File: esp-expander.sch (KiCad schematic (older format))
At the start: 0 parts

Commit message: Added labels
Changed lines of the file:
@@
 $EndDescr
 $Sheet
-S 4950 2700 1750 1850
+S 4250 2550 2250 3350
 U 6212150F
 F0 "ESP32" 50
 F1 "ESP32.sch" 50
+F2 "RESET" I L 4250 2650 50
+F3 "PROG_GPIO0" I L 4250 2750 50
+F4 "PROG_TX" I L 4250 2850 50
+F5 "PROG_RX" I L 4250 2950 50
+F6 "I2C_SCL" I R 6500 2750 50
+F7 "I2C_SDA" I R 6500 2650 50
+F8 "LAN_CLKIN" I L 4250 3250 50
+F9 "LAN_MDC" I L 4250 3350 50
+F10 "LAN_MDIO" I L 4250 3450 50
+F11 "LAN_MODE2" I L 4250 3550 50
+F12 "LAN_MODE1" I L 4250 3650 50
+F13 "LAN_MODE0" I L 4250 3750 50
+F14 "LAN_TXEN" I L 4250 3850 50
+F15 "LAN_TXED1" I L 4250 3950 50
+F16 "LAN_TXED0" I L 4250 4050 50
+F17 "LAN_RESET" I L 4250 4150 50
+F18 "DIGITAL_1" I L 4250 4450 50
+F19 "DIGITAL_2" I L 4250 4550 50
+F20 "DIGITAL_3" I L 4250 4650 50
+F21 "DIGITAL_4" I L 4250 4750 50
+F22 "DIGITAL_5" I L 4250 4850 50
+F23 "MCP_INTA" I R 6500 2850 50
+F24 "MCP_INTB" I R 6500 2950 50
 $EndSheet
 $Sheet
-S 2050 2000 900  1050
+S 4250 1250 900  1050
 U 6213DFD4
 F0 "Power" 50
@@
 $EndSheet
 $Sheet
-S 2250 4850 850  1650
+S 6550 2550 850  1650
 U 6215A73B
 F0 "MCP" 50
 F1 "MCP.sch" 50
+F2 "SDA" I L 6550 2650 50
+F3 "SCL" I L 6550 2750 50
+F4 "INTB" I L 6550 2950 50
+F5 "INTA" I L 6550 2850 50
+F6 "MCP1" I R 7400 2650 50
+F7 "MCP2" I R 7400 2750 50
+F8 "MCP3" I R 7400 2850 50
+F9 "MCP4" I R 7400 2950 50
+F10 "MCP5" I R 7400 3050 50
+F11 "MCP6" I R 7400 3150 50
+F12 "MCP7" I R 7400 3250 50
+F13 "MCP8" I R 7400 3350 50
+F14 "MCP9" I R 7400 3450 50
+F15 "MCP10" I R 7400 3550 50
+F16 "MCP11" I R 7400 3650 50
+F17 "MCP12" I R 7400 3750 50
+F18 "MCP13" I R 7400 3850 50
+F19 "MCP14" I R 7400 3950 50
+F20 "MCP15" I R 7400 4050 50
+F21 "MCP16" I R 7400 4150 50
 $EndSheet
 $EndSCHEMATC

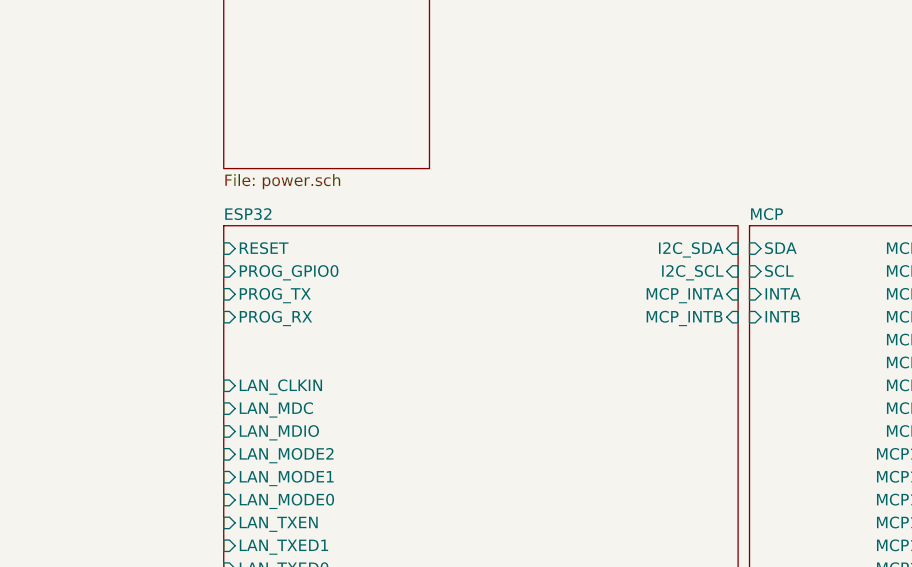
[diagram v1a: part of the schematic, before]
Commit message: Added programming port
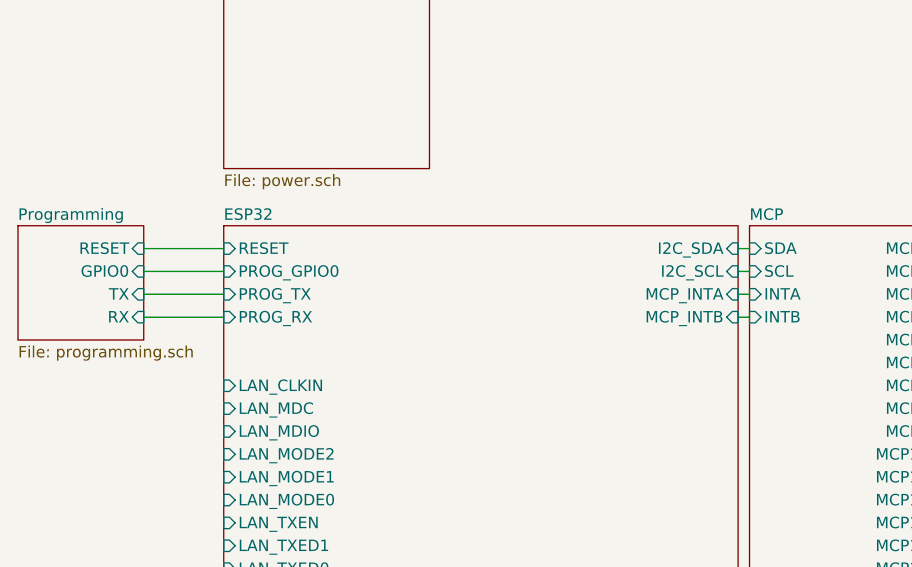
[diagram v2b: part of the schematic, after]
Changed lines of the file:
@@
 $Descr A4 11693 8268
 encoding utf-8
-Sheet 1 4
+Sheet 1 5
 Title "ESP Expander"
 Date "2022-02-20"
@@
 F21 "MCP16" I R 7400 4150 50
 $EndSheet
+$Sheet
+S 3350 2550 550  500
+U 62173728
+F0 "Programming" 50
+F1 "programming.sch" 50
+F2 "RX" I R 3900 2950 50
+F3 "TX" I R 3900 2850 50
+F4 "GPIO0" I R 3900 2750 50
+F5 "RESET" I R 3900 2650 50
+$EndSheet
+Wire Wire Line
+	3900 2650 4250 2650
+Wire Wire Line
+	4250 2750 3900 2750
+Wire Wire Line
+	3900 2850 4250 2850
+Wire Wire Line
+	4250 2950 3900 2950
+Wire Wire Line
+	6500 2650 6550 2650
+Wire Wire Line
+	6500 2750 6550 2750
+Wire Wire Line
+	6500 2850 6550 2850
+Wire Wire Line
+	6500 2950 6550 2950
 $EndSCHEMATC

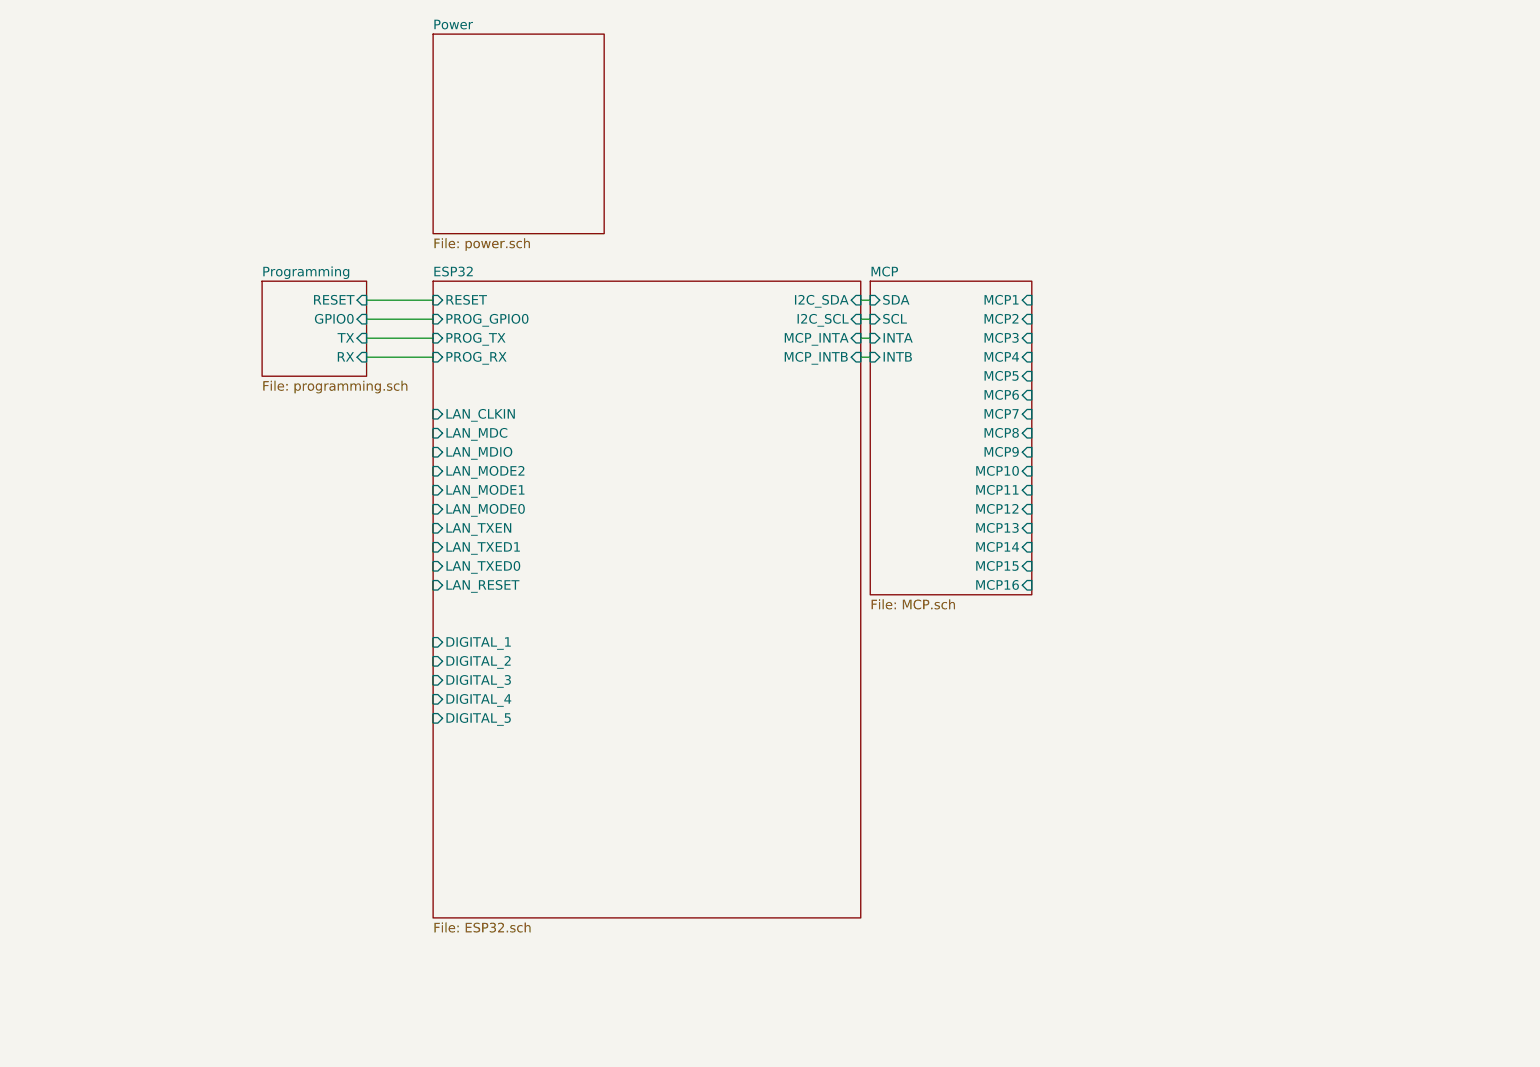
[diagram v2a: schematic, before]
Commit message: Added LAN circuit
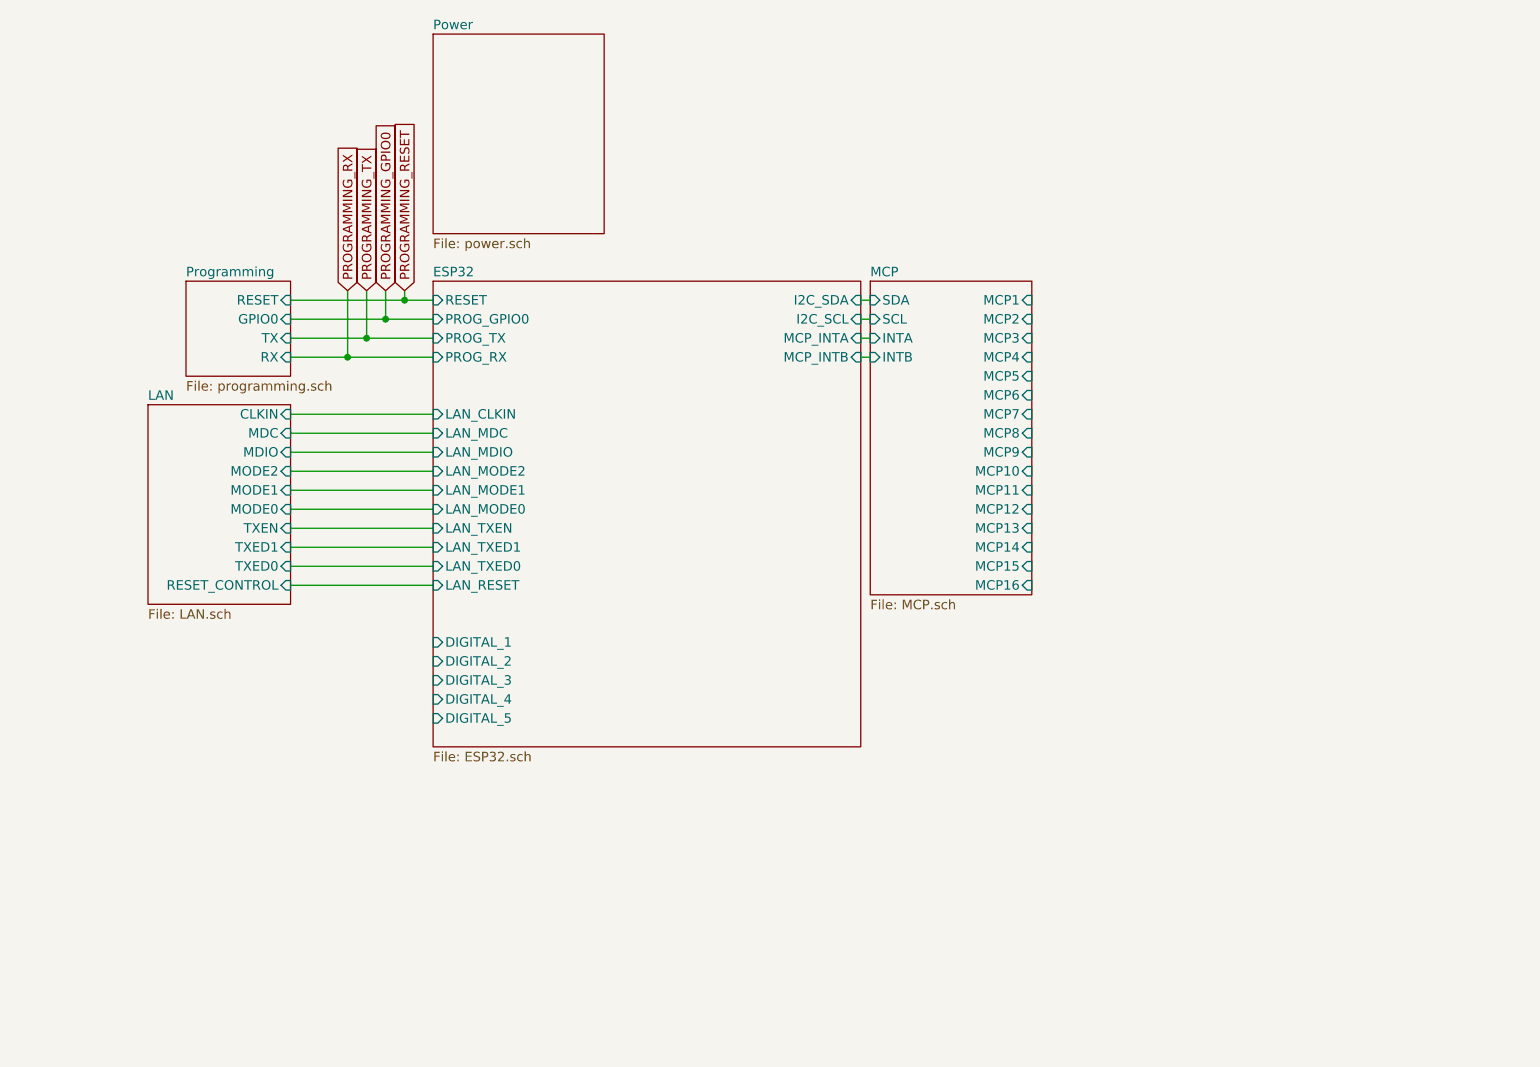
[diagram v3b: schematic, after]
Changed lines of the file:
@@
 $Descr A4 11693 8268
 encoding utf-8
-Sheet 1 5
+Sheet 1 6
 Title "ESP Expander"
 Date "2022-02-20"
@@
 $EndDescr
 $Sheet
-S 4250 2550 2250 3350
+S 4250 2550 2250 2450
 U 6212150F
 F0 "ESP32" 50
@@
 $EndSheet
 $Sheet
-S 3350 2550 550  500
+S 2950 2550 550  500
 U 62173728
 F0 "Programming" 50
 F1 "programming.sch" 50
-F2 "RX" I R 3900 2950 50
-F3 "TX" I R 3900 2850 50
-F4 "GPIO0" I R 3900 2750 50
-F5 "RESET" I R 3900 2650 50
+F2 "RX" I R 3500 2950 50
+F3 "TX" I R 3500 2850 50
+F4 "GPIO0" I R 3500 2750 50
+F5 "RESET" I R 3500 2650 50
 $EndSheet
-Wire Wire Line
-	3900 2650 4250 2650
-Wire Wire Line
-	4250 2750 3900 2750
-Wire Wire Line
-	3900 2850 4250 2850
-Wire Wire Line
-	4250 2950 3900 2950
 Wire Wire Line
 	6500 2650 6550 2650
@@
 Wire Wire Line
 	6500 2950 6550 2950
+$Sheet
+S 2750 3200 750  1050
+U 62182BE5
+F0 "LAN" 50
+F1 "LAN.sch" 50
+F2 "TXED0" I R 3500 4050 50
+F3 "TXED1" I R 3500 3950 50
+F4 "TXEN" I R 3500 3850 50
+F5 "MODE0" I R 3500 3750 50
+F6 "MODE1" I R 3500 3650 50
+F7 "MODE2" I R 3500 3550 50
+F8 "MDIO" I R 3500 3450 50
+F9 "MDC" I R 3500 3350 50
+F10 "CLKIN" I R 3500 3250 50
+F11 "RESET_CONTROL" I R 3500 4150 50
+$EndSheet
+Text GLabel 4100 2600 1    50   Input ~ 0
+PROGRAMMING_RESET
+Text GLabel 4000 2600 1    50   Input ~ 0
+PROGRAMMING_GPIO0
+Text GLabel 3900 2600 1    50   Input ~ 0
+PROGRAMMING_TX
+Text GLabel 3800 2600 1    50   Input ~ 0
+PROGRAMMING_RX
+Wire Wire Line
+	3500 2750 4000 2750
+Wire Wire Line
+	3500 2850 3900 2850
+Wire Wire Line
+	3500 2950 3800 2950
+Wire Wire Line
+	4100 2600 4100 2650
+Connection ~ 4100 2650
+Wire Wire Line
+	4100 2650 4250 2650
+Wire Wire Line
+	4000 2600 4000 2750
+Connection ~ 4000 2750
+Wire Wire Line
+	4000 2750 4250 2750
+Wire Wire Line
+	3900 2600 3900 2850
+Connection ~ 3900 2850
+Wire Wire Line
+	3900 2850 4250 2850
+Wire Wire Line
+	3500 2650 4100 2650
+Wire Wire Line
+	3800 2600 3800 2950
+Connection ~ 3800 2950
+Wire Wire Line
+	3800 2950 4250 2950
+Wire Wire Line
+	3500 3250 4250 3250
+Wire Wire Line
+	4250 3350 3500 3350
+Wire Wire Line
+	3500 3450 4250 3450
+Wire Wire Line
+	4250 3550 3500 3550
+Wire Wire Line
+	3500 3650 4250 3650
+Wire Wire Line
+	4250 3750 3500 3750
+Wire Wire Line
+	3500 3850 4250 3850
+Wire Wire Line
+	4250 3950 3500 3950
+Wire Wire Line
+	3500 4050 4250 4050
+Wire Wire Line
+	4250 4150 3500 4150
 $EndSCHEMATC

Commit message: Added lcsc part nums
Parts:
- added J3, J4: Conn_01x16, Connector_PinHeader_2.54mm:PinHeader_1x16_P2.54mm_Vertical, symbol Connector_Generic:Conn_01x16
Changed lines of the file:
@@
 Wire Wire Line
 	4250 4150 3500 4150
+$Comp
+L Connector_Generic:Conn_01x16 J3
+U 1 1 6223BC0D
+P 9400 2900
+F 0 "J3" H 9480 2892 50  0000 L CNN
+F 1 "Conn_01x16" H 9480 2801 50  0000 L CNN
+F 2 "Connector_PinHeader_2.54mm:PinHeader_1x16_P2.54mm_Vertical" H 9400 2900 50  0001 C CNN
+F 3 "~" H 9400 2900 50  0001 C CNN
+	1    9400 2900
+	1    0    0    -1
+$EndComp
+$Comp
+L Connector_Generic:Conn_01x16 J4
+U 1 1 6223C85B
+P 9400 4700
+F 0 "J4" H 9480 4692 50  0000 L CNN
+F 1 "Conn_01x16" H 9480 4601 50  0000 L CNN
+F 2 "Connector_PinHeader_2.54mm:PinHeader_1x16_P2.54mm_Vertical" H 9400 4700 50  0001 C CNN
+F 3 "~" H 9400 4700 50  0001 C CNN
+	1    9400 4700
+	1    0    0    -1
+$EndComp
 $EndSCHEMATC

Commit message: Added schematic
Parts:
- removed J4: Conn_01x16, Connector_PinHeader_2.54mm:PinHeader_1x16_P2.54mm_Vertical, symbol Connector_Generic:Conn_01x16
- added J4: Conn_01x12, Connector_PinHeader_2.54mm:PinHeader_1x12_P2.54mm_Vertical, symbol Connector_Generic:Conn_01x12
- J3: footprint Connector_PinHeader_2.54mm:PinHeader_1x16_P2.54mm_Vertical -> Connector_PinHeader_2.54mm:PinHeader_1x18_P2.54mm_Vertical; symbol Connector_Generic:Conn_01x16 -> Connector_Generic:Conn_01x18; LCSC (none) -> C725948
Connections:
- net MCP/MCP1: now also J3.2 (Pin_2)
- net MCP/MCP10: now also J3.11 (Pin_11)
- net MCP/MCP11: now also J3.12 (Pin_12)
- net MCP/MCP12: now also J3.13 (Pin_13)
- net MCP/MCP13: now also J3.14 (Pin_14)
- net MCP/MCP14: now also J3.15 (Pin_15)
- net MCP/MCP15: now also J3.16 (Pin_16)
- net MCP/MCP16: now also J3.17 (Pin_17)
- net MCP/MCP2: now also J3.3 (Pin_3)
- net MCP/MCP3: now also J3.4 (Pin_4)
- net MCP/MCP4: now also J3.5 (Pin_5)
- net MCP/MCP5: now also J3.6 (Pin_6)
- net MCP/MCP6: now also J3.7 (Pin_7)
- net MCP/MCP7: now also J3.8 (Pin_8)
- net MCP/MCP8: now also J3.9 (Pin_9)
- net MCP/MCP9: now also J3.10 (Pin_10)
- net PROGRAMMING_GPIO0: now also J4.10 (Pin_10)
- net PROGRAMMING_RESET: now also J4.9 (Pin_9)
- net PROGRAMMING_RX: now also J4.12 (Pin_12)
- net PROGRAMMING_TX: now also J4.11 (Pin_11)
- net +3V3: now reaches J3.1 (Pin_1)
- net +3V3: now also J4.3 (Pin_3)
- new net DIGITAL1: J4.4 (Pin_4)
- new net DIGITAL2: J4.5 (Pin_5)
- new net DIGITAL3: J4.6 (Pin_6)
- new net DIGITAL4: J4.7 (Pin_7)
- new net DIGITAL5: J4.8 (Pin_8)
- new net GND: J3.18 (Pin_18), J4.2 (Pin_2)
- new net VCC: J4.1 (Pin_1)
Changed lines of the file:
@@
 	4250 4150 3500 4150
 $Comp
-L Connector_Generic:Conn_01x16 J3
+L Connector_Generic:Conn_01x18 J3
 U 1 1 6223BC0D
-P 9400 2900
-F 0 "J3" H 9480 2892 50  0000 L CNN
-F 1 "Conn_01x16" H 9480 2801 50  0000 L CNN
-F 2 "Connector_PinHeader_2.54mm:PinHeader_1x16_P2.54mm_Vertical" H 9400 2900 50  0001 C CNN
-F 3 "~" H 9400 2900 50  0001 C CNN
-	1    9400 2900
+P 7650 3350
+F 0 "J3" V 7750 4000 50  0000 L CNN
+F 1 "Conn_01x16" V 7750 2550 50  0000 L CNN
+F 2 "Connector_PinHeader_2.54mm:PinHeader_1x18_P2.54mm_Vertical" H 7650 3350 50  0001 C CNN
+F 3 "~" H 7650 3350 50  0001 C CNN
+F 4 "C725948" H 7650 3350 50  0001 C CNN "LCSC"
+	1    7650 3350
+	1    0    0    -1
+$EndComp
+Wire Wire Line
+	7400 2650 7450 2650
+Wire Wire Line
+	7400 2750 7450 2750
+Wire Wire Line
+	7400 2850 7450 2850
+Wire Wire Line
+	7400 2950 7450 2950
+Wire Wire Line
+	7400 3050 7450 3050
+Wire Wire Line
+	7400 3150 7450 3150
+Wire Wire Line
+	7400 3250 7450 3250
+Wire Wire Line
+	7400 3350 7450 3350
+Wire Wire Line
+	7400 3450 7450 3450
+Wire Wire Line
+	7400 3550 7450 3550
+Wire Wire Line
+	7400 3650 7450 3650
+Wire Wire Line
+	7400 3750 7450 3750
+Wire Wire Line
+	7400 3850 7450 3850
+Wire Wire Line
+	7400 3950 7450 3950
+Wire Wire Line
+	7400 4050 7450 4050
+Wire Wire Line
+	7400 4150 7450 4150
+Text GLabel 7400 5650 0    50   Input ~ 0
+PROGRAMMING_RESET
+Text GLabel 7400 5750 0    50   Input ~ 0
+PROGRAMMING_GPIO0
+Text GLabel 7400 5850 0    50   Input ~ 0
+PROGRAMMING_TX
+Text GLabel 7400 5950 0    50   Input ~ 0
+PROGRAMMING_RX
+Text GLabel 4200 4450 0    50   Input ~ 0
+DIGITAL1
+Text GLabel 4200 4550 0    50   Input ~ 0
+DIGITAL2
+Text GLabel 4200 4650 0    50   Input ~ 0
+DIGITAL3
+Text GLabel 4200 4750 0    50   Input ~ 0
+DIGITAL4
+Text GLabel 4200 4850 0    50   Input ~ 0
+DIGITAL5
+Wire Wire Line
+	4200 4450 4250 4450
+Wire Wire Line
+	4250 4550 4200 4550
+Wire Wire Line
+	4250 4650 4200 4650
+Wire Wire Line
+	4250 4750 4200 4750
+Wire Wire Line
+	4250 4850 4200 4850
+Text GLabel 7400 5150 0    50   Input ~ 0
+DIGITAL1
+Text GLabel 7400 5250 0    50   Input ~ 0
+DIGITAL2
+Text GLabel 7400 5350 0    50   Input ~ 0
+DIGITAL3
+Text GLabel 7400 5450 0    50   Input ~ 0
+DIGITAL4
+Text GLabel 7400 5550 0    50   Input ~ 0
+DIGITAL5
+$Comp
+L power:VCC #PWR0150
+U 1 1 62167D5E
+P 7400 4850
+F 0 "#PWR0150" H 7400 4700 50  0001 C CNN
+F 1 "VCC" V 7415 4977 50  0000 L CNN
+F 2 "" H 7400 4850 50  0001 C CNN
+F 3 "" H 7400 4850 50  0001 C CNN
+	1    7400 4850
+	0    -1   -1   0
+$EndComp
+$Comp
+L power:GND #PWR0151
+U 1 1 62168614
+P 7400 4950
+F 0 "#PWR0151" H 7400 4700 50  0001 C CNN
+F 1 "GND" V 7405 4822 50  0000 R CNN
+F 2 "" H 7400 4950 50  0001 C CNN
+F 3 "" H 7400 4950 50  0001 C CNN
+	1    7400 4950
+	0    1    1    0
+$EndComp
+$Comp
+L power:+3.3V #PWR0152
+U 1 1 62168D33
+P 7400 5050
+F 0 "#PWR0152" H 7400 4900 50  0001 C CNN
+F 1 "+3.3V" V 7415 5178 50  0000 L CNN
+F 2 "" H 7400 5050 50  0001 C CNN
+F 3 "" H 7400 5050 50  0001 C CNN
+	1    7400 5050
+	0    -1   -1   0
+$EndComp
+Wire Wire Line
+	7400 5650 7450 5650
+Wire Wire Line
+	7450 5750 7400 5750
+Wire Wire Line
+	7400 5850 7450 5850
+Wire Wire Line
+	7400 5950 7450 5950
+Wire Wire Line
+	7400 5550 7450 5550
+Wire Wire Line
+	7400 5450 7450 5450
+Wire Wire Line
+	7400 5350 7450 5350
+Wire Wire Line
+	7400 5250 7450 5250
+Wire Wire Line
+	7400 5150 7450 5150
+$Comp
+L Connector_Generic:Conn_01x12 J4
+U 1 1 621788BD
+P 7650 5350
+F 0 "J4" H 7730 5342 50  0000 L CNN
+F 1 "Conn_01x12" H 7730 5251 50  0000 L CNN
+F 2 "Connector_PinHeader_2.54mm:PinHeader_1x12_P2.54mm_Vertical" H 7650 5350 50  0001 C CNN
+F 3 "~" H 7650 5350 50  0001 C CNN
+F 4 "C225487" H 7650 5350 50  0001 C CNN "LCSC"
+	1    7650 5350
+	1    0    0    -1
+$EndComp
+Wire Wire Line
+	7450 4850 7400 4850
+Wire Wire Line
+	7450 4950 7400 4950
+Wire Wire Line
+	7450 5050 7400 5050
+$Comp
+L power:GND #PWR0153
+U 1 1 6218591A
+P 7400 4300
+F 0 "#PWR0153" H 7400 4050 50  0001 C CNN
+F 1 "GND" H 7405 4127 50  0000 C CNN
+F 2 "" H 7400 4300 50  0001 C CNN
+F 3 "" H 7400 4300 50  0001 C CNN
+	1    7400 4300
 	1    0    0    -1
 $EndComp
 $Comp
-L Connector_Generic:Conn_01x16 J4
-U 1 1 6223C85B
-P 9400 4700
-F 0 "J4" H 9480 4692 50  0000 L CNN
-F 1 "Conn_01x16" H 9480 4601 50  0000 L CNN
-F 2 "Connector_PinHeader_2.54mm:PinHeader_1x16_P2.54mm_Vertical" H 9400 4700 50  0001 C CNN
-F 3 "~" H 9400 4700 50  0001 C CNN
-	1    9400 4700
+L power:+3.3V #PWR0154
+U 1 1 62185DAA
+P 7400 2500
+F 0 "#PWR0154" H 7400 2350 50  0001 C CNN
+F 1 "+3.3V" H 7415 2673 50  0000 C CNN
+F 2 "" H 7400 2500 50  0001 C CNN
+F 3 "" H 7400 2500 50  0001 C CNN
+	1    7400 2500
 	1    0    0    -1
 $EndComp
+Wire Wire Line
+	7400 4300 7400 4250
+Wire Wire Line
+	7400 4250 7450 4250
+Wire Wire Line
+	7400 2500 7400 2550
+Wire Wire Line
+	7400 2550 7450 2550
 $EndSCHEMATC
